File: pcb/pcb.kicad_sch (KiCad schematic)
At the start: 57 parts, among them J1 N!N, J2 Conn_01x02_Socket, J4 Display_nice-view, J8 Conn_01x12_Socket, J9 Conn_01x12_Socket, SW10 Switch, SW11 Switch, SW12 Switch, SW13 Switch, SW14 Switch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

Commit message: small updates
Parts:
- D10, D11, D12, D13, D14, D15, D19, D20, D3, D4, D5, D6, D7, D8, D9: footprint zzkeeb:Diode_1N4148-SOD123-reversible -> zzkeeb:Diode_1N4148-SOD123-reversible-flip3d
- J8, J9: footprint Connector_FFC-FPC:TE_1-84952-2_1x12-1MP_P1.0mm_Horizontal -> zzkeeb:Connector_FFC-12pin-1mm-horizontal
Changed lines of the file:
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@@
       (effects (font (size 1.27 1.27)) (justify right) hide)
     )
-    (property "Footprint" "zzkeeb:Diode_1N4148-SOD123-reversible" (at 66.04 96.52 90)
+    (property "Footprint" "zzkeeb:Diode_1N4148-SOD123-reversible-flip3d" (at 66.04 96.52 90)
       (effects (font (size 1.27 1.27)) hide)
     )
@@
       (effects (font (size 1.27 1.27)) (justify right) hide)
     )
-    (property "Footprint" "zzkeeb:Diode_1N4148-SOD123-reversible" (at 83.82 137.16 90)
+    (property "Footprint" "zzkeeb:Diode_1N4148-SOD123-reversible-flip3d" (at 83.82 137.16 90)
       (effects (font (size 1.27 1.27)) hide)
     )
@@
       (effects (font (size 1.27 1.27)) (justify right) hide)
     )
-    (property "Footprint" "zzkeeb:Diode_1N4148-SOD123-reversible" (at 30.48 96.52 90)
+    (property "Footprint" "zzkeeb:Diode_1N4148-SOD123-reversible-flip3d" (at 30.48 96.52 90)
       (effects (font (size 1.27 1.27)) hide)
     )
@@
       (effects (font (size 1.27 1.27)) (justify right) hide)
     )
-    (property "Footprint" "zzkeeb:Diode_1N4148-SOD123-reversible" (at 30.48 116.84 90)
+    (property "Footprint" "zzkeeb:Diode_1N4148-SOD123-reversible-flip3d" (at 30.48 116.84 90)
       (effects (font (size 1.27 1.27)) hide)
     )
@@
       (effects (font (size 1.27 1.27)) (justify right) hide)
     )
-    (property "Footprint" "zzkeeb:Diode_1N4148-SOD123-reversible" (at 66.04 116.84 90)
+    (property "Footprint" "zzkeeb:Diode_1N4148-SOD123-reversible-flip3d" (at 66.04 116.84 90)
       (effects (font (size 1.27 1.27)) hide)
     )
@@
       (effects (font (size 1.27 1.27)) (justify right) hide)
     )
-    (property "Footprint" "zzkeeb:Diode_1N4148-SOD123-reversible" (at 66.04 137.16 90)
+    (property "Footprint" "zzkeeb:Diode_1N4148-SOD123-reversible-flip3d" (at 66.04 137.16 90)
       (effects (font (size 1.27 1.27)) hide)
     )
@@
       (effects (font (size 1.27 1.27)) (justify right) hide)
     )
-    (property "Footprint" "zzkeeb:Diode_1N4148-SOD123-reversible" (at 48.26 116.84 90)
+    (property "Footprint" "zzkeeb:Diode_1N4148-SOD123-reversible-flip3d" (at 48.26 116.84 90)
       (effects (font (size 1.27 1.27)) hide)
     )
@@
       (effects (font (size 1.27 1.27)) (justify left))
     )
-    (property "Footprint" "Connector_FFC-FPC:TE_1-84952-2_1x12-1MP_P1.0mm_Horizontal" (at 196.85 83.82 0)
+    (property "Footprint" "zzkeeb:Connector_FFC-12pin-1mm-horizontal" (at 196.85 83.82 0)
       (effects (font (size 1.27 1.27)) hide)
     )
@@
       (effects (font (size 1.27 1.27)) (justify right) hide)
     )
-    (property "Footprint" "zzkeeb:Diode_1N4148-SOD123-reversible" (at 48.26 96.52 90)
+    (property "Footprint" "zzkeeb:Diode_1N4148-SOD123-reversible-flip3d" (at 48.26 96.52 90)
       (effects (font (size 1.27 1.27)) hide)
     )
@@
       (effects (font (size 1.27 1.27)) (justify right) hide)
     )
-    (property "Footprint" "zzkeeb:Diode_1N4148-SOD123-reversible" (at 30.48 137.16 90)
+    (property "Footprint" "zzkeeb:Diode_1N4148-SOD123-reversible-flip3d" (at 30.48 137.16 90)
       (effects (font (size 1.27 1.27)) hide)
     )
@@
       (effects (font (size 1.27 1.27)) (justify left))
     )
-    (property "Footprint" "Connector_FFC-FPC:TE_1-84952-2_1x12-1MP_P1.0mm_Horizontal" (at 245.11 83.82 0)
+    (property "Footprint" "zzkeeb:Connector_FFC-12pin-1mm-horizontal" (at 245.11 83.82 0)
       (effects (font (size 1.27 1.27)) hide)
     )
@@
       (effects (font (size 1.27 1.27)) (justify right) hide)
     )
-    (property "Footprint" "zzkeeb:Diode_1N4148-SOD123-reversible" (at 83.82 96.52 90)
+    (property "Footprint" "zzkeeb:Diode_1N4148-SOD123-reversible-flip3d" (at 83.82 96.52 90)
       (effects (font (size 1.27 1.27)) hide)
     )
@@
       (effects (font (size 1.27 1.27)) (justify right) hide)
     )
-    (property "Footprint" "zzkeeb:Diode_1N4148-SOD123-reversible" (at 83.82 157.48 90)
+    (property "Footprint" "zzkeeb:Diode_1N4148-SOD123-reversible-flip3d" (at 83.82 157.48 90)
       (effects (font (size 1.27 1.27)) hide)
     )
@@
       (effects (font (size 1.27 1.27)) (justify right) hide)
     )
-    (property "Footprint" "zzkeeb:Diode_1N4148-SOD123-reversible" (at 101.6 96.52 90)
+    (property "Footprint" "zzkeeb:Diode_1N4148-SOD123-reversible-flip3d" (at 101.6 96.52 90)
       (effects (font (size 1.27 1.27)) hide)
     )
@@
       (effects (font (size 1.27 1.27)) (justify right) hide)
     )
-    (property "Footprint" "zzkeeb:Diode_1N4148-SOD123-reversible" (at 48.26 157.48 90)
+    (property "Footprint" "zzkeeb:Diode_1N4148-SOD123-reversible-flip3d" (at 48.26 157.48 90)
       (effects (font (size 1.27 1.27)) hide)
     )
@@
       (effects (font (size 1.27 1.27)) (justify right) hide)
     )
-    (property "Footprint" "zzkeeb:Diode_1N4148-SOD123-reversible" (at 101.6 116.84 90)
+    (property "Footprint" "zzkeeb:Diode_1N4148-SOD123-reversible-flip3d" (at 101.6 116.84 90)
       (effects (font (size 1.27 1.27)) hide)
     )
@@
       (effects (font (size 1.27 1.27)) (justify right) hide)
     )
-    (property "Footprint" "zzkeeb:Diode_1N4148-SOD123-reversible" (at 66.04 157.48 90)
+    (property "Footprint" "zzkeeb:Diode_1N4148-SOD123-reversible-flip3d" (at 66.04 157.48 90)
       (effects (font (size 1.27 1.27)) hide)
     )
@@
       (effects (font (size 1.27 1.27)) (justify right) hide)
     )
-    (property "Footprint" "zzkeeb:Diode_1N4148-SOD123-reversible" (at 83.82 116.84 90)
+    (property "Footprint" "zzkeeb:Diode_1N4148-SOD123-reversible-flip3d" (at 83.82 116.84 90)
       (effects (font (size 1.27 1.27)) hide)
     )
@@
       (effects (font (size 1.27 1.27)) (justify right) hide)
     )
-    (property "Footprint" "zzkeeb:Diode_1N4148-SOD123-reversible" (at 101.6 157.48 90)
+    (property "Footprint" "zzkeeb:Diode_1N4148-SOD123-reversible-flip3d" (at 101.6 157.48 90)
       (effects (font (size 1.27 1.27)) hide)
     )
@@
       (effects (font (size 1.27 1.27)) (justify right) hide)
     )
-    (property "Footprint" "zzkeeb:Diode_1N4148-SOD123-reversible" (at 48.26 137.16 90)
+    (property "Footprint" "zzkeeb:Diode_1N4148-SOD123-reversible-flip3d" (at 48.26 137.16 90)
       (effects (font (size 1.27 1.27)) hide)
     )
@@
       (effects (font (size 1.27 1.27)) (justify right) hide)
     )
-    (property "Footprint" "zzkeeb:Diode_1N4148-SOD123-reversible" (at 101.6 137.16 90)
+    (property "Footprint" "zzkeeb:Diode_1N4148-SOD123-reversible-flip3d" (at 101.6 137.16 90)
       (effects (font (size 1.27 1.27)) hide)
     )
@@
       (effects (font (size 1.27 1.27)) (justify right) hide)
     )
-    (property "Footprint" "zzkeeb:Diode_1N4148-SOD123-reversible" (at 30.48 157.48 90)
-      (effects (font (size 1.27 1.27)) hide)
-    )
+    (property "Footprint" "zzkeeb:Diode_1N4148-SOD123-reversible-flip3d" (at 30.48 157.48 90)
+      (effects (font (size 1.27 1.27)) hide)
+    )

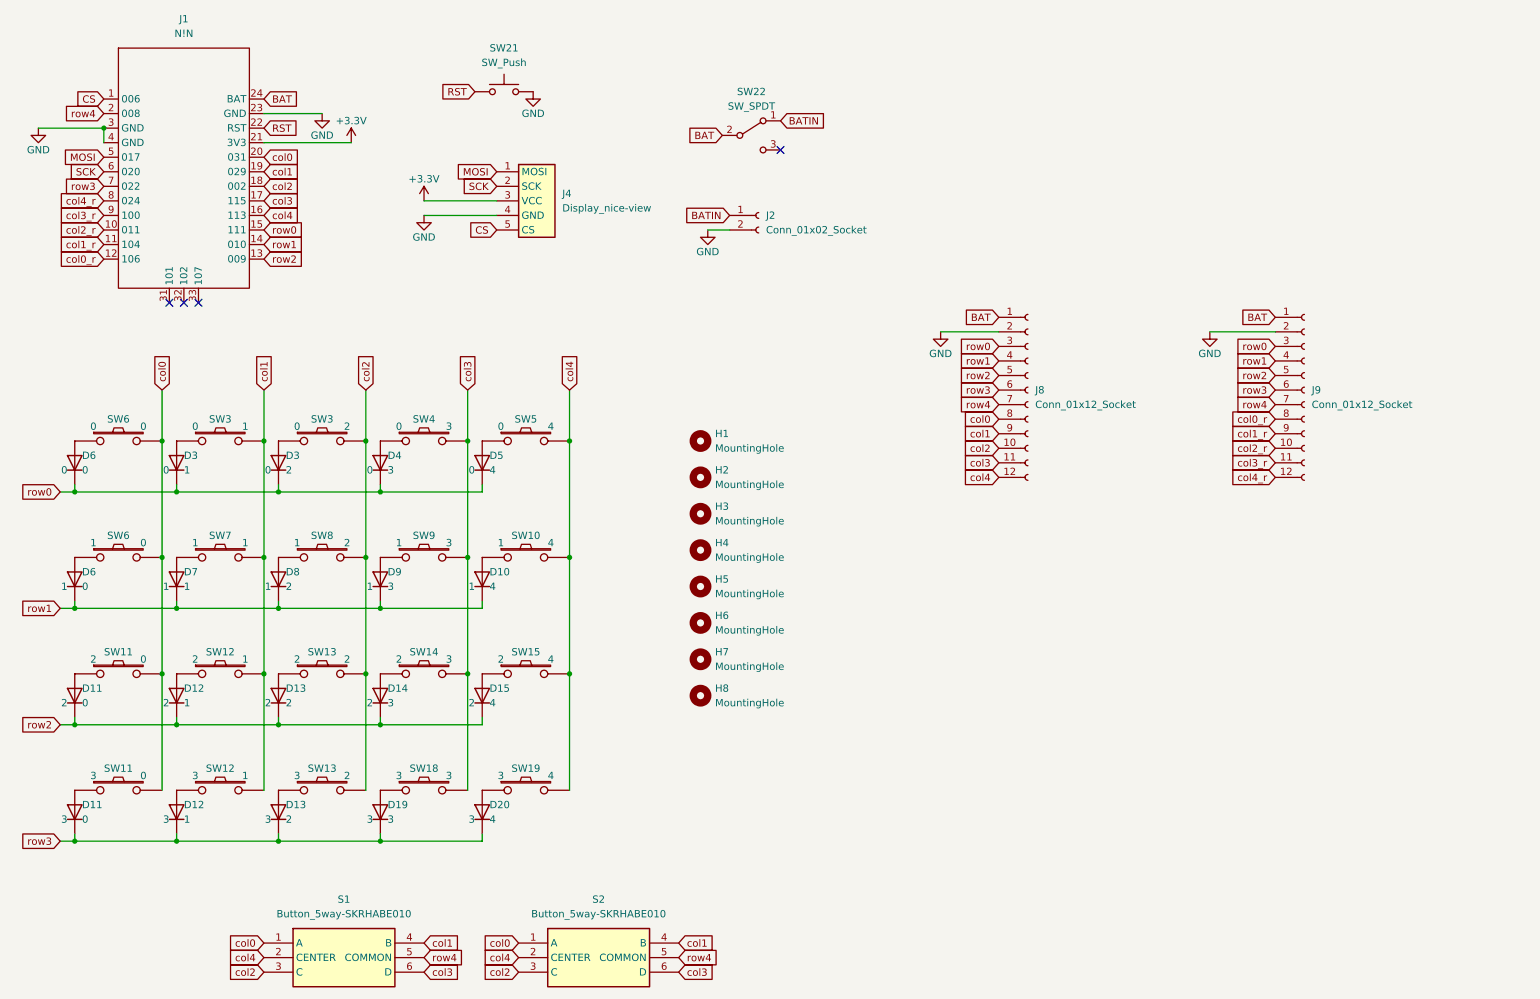
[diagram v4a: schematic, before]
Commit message: move mcu to right, add encoder
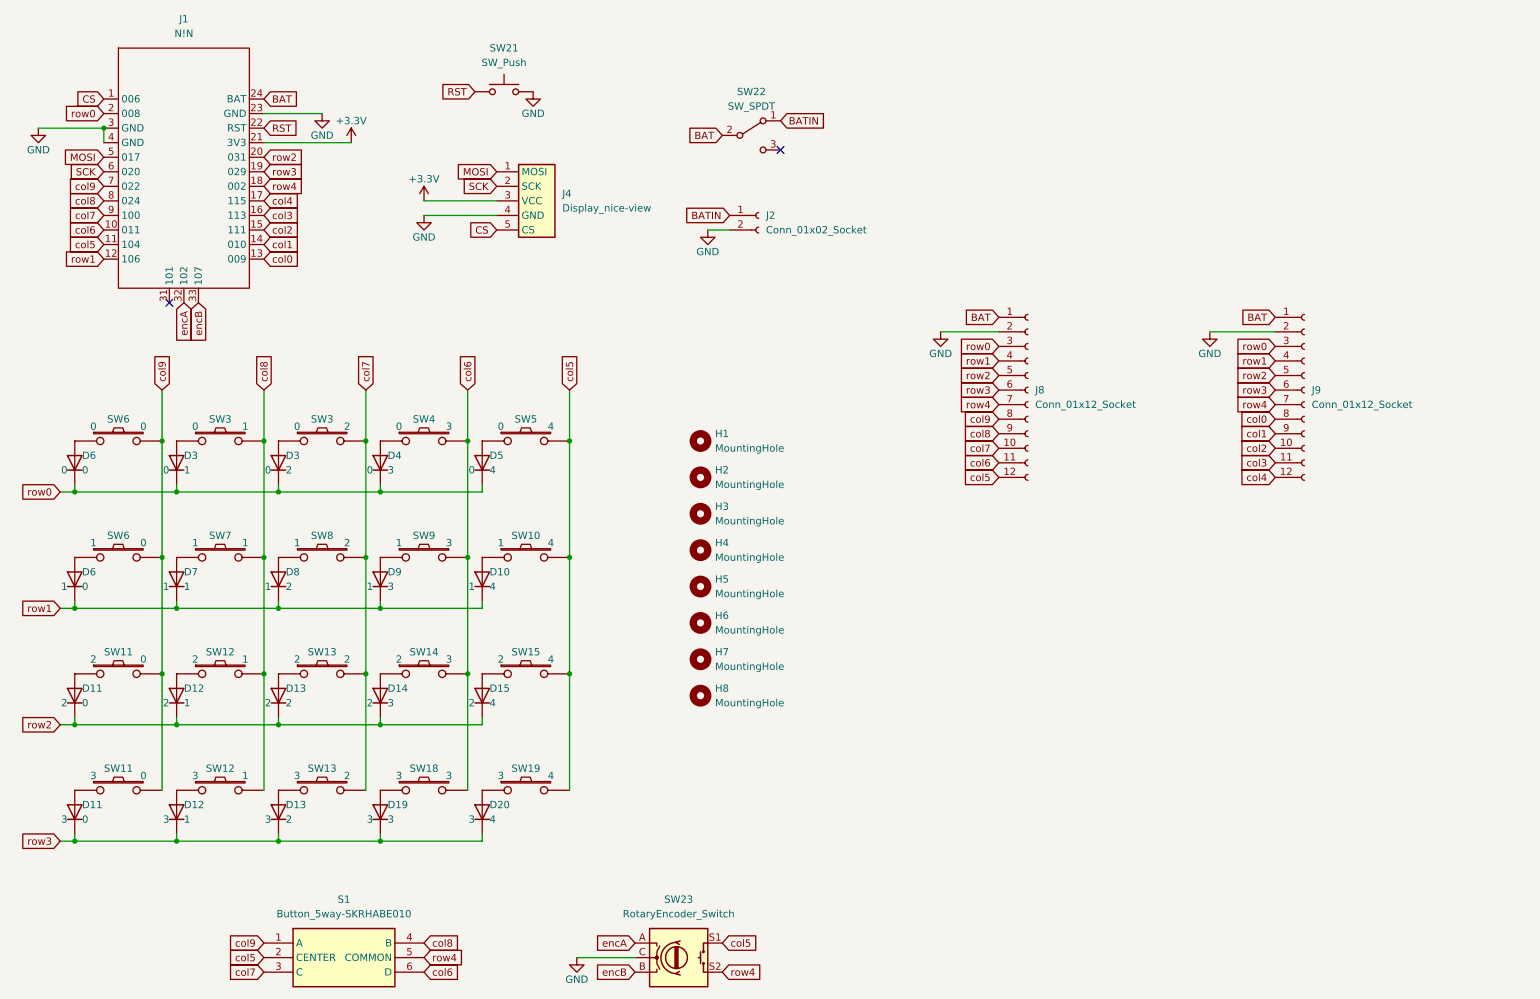
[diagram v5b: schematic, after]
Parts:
- removed S2: Button_5way-SKRHABE010, zzkeeb:Button_5way-SKRHABE010, symbol zzkeeb:Button_5way-SKRHABE010
- added SW23: RotaryEncoder_Switch, zzkeeb:RotaryEncoder_EC11, symbol Device:RotaryEncoder_Switch
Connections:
- net GND: now also SW23.C
- net col0: now also J1.13 (009), J9.8 (Pin_8); no longer J1.20 (031), J8.8 (Pin_8), S1.1 (A), SW11.2, SW11.2, SW6.2, SW6.2
- net col1: now also J1.14 (010), J9.9 (Pin_9); no longer J1.19 (029), J8.9 (Pin_9), S1.4 (B), SW12.2, SW12.2, SW3.2, SW7.2
- net col2: now also J1.15 (111), J9.10 (Pin_10); no longer J1.18 (002), J8.10 (Pin_10), S1.3 (C), SW13.2, SW13.2, SW3.2, SW8.2
- net col3: now also J1.16 (113), J9.11 (Pin_11); no longer J1.17 (115), J8.11 (Pin_11), S1.6 (D), SW14.2, SW18.2, SW4.2, SW9.2
- net col4: now also J1.17 (115), J9.12 (Pin_12); no longer J1.16 (113), J8.12 (Pin_12), S1.2 (CENTER), SW10.2, SW15.2, SW19.2, SW5.2
- net row0: now also J1.2 (008); no longer J1.15 (111)
- net row1: now also J1.12 (106); no longer J1.14 (010)
- net row2: now also J1.20 (031); no longer J1.13 (009)
- net row3: now also J1.19 (029); no longer J1.7 (022)
- net row4: now also J1.18 (002), SW23.S2; no longer J1.2 (008)
- net encA: now reaches J1.32 (102)
- net encA: now also SW23.A
- net encB: now reaches J1.33 (107)
- net encB: now also SW23.B
- removed net col0_r: J1.12 (106), J9.8 (Pin_8)
- net col1_r renamed col5
- net col5: now also J8.12 (Pin_12), S1.2 (CENTER), SW10.2, SW15.2, SW19.2, SW5.2, SW23.S1; no longer J9.9 (Pin_9)
- net col2_r renamed col6
- net col6: now also J8.11 (Pin_11), S1.6 (D), SW14.2, SW18.2, SW4.2, SW9.2; no longer J9.10 (Pin_10)
- net col3_r renamed col7
- net col7: now also J8.10 (Pin_10), S1.3 (C), SW13.2, SW13.2, SW3.2, SW8.2; no longer J9.11 (Pin_11)
- net col4_r renamed col8
- net col8: now also J8.9 (Pin_9), S1.4 (B), SW12.2, SW12.2, SW3.2, SW7.2; no longer J9.12 (Pin_12)
- new net col9: J1.7 (022), J8.8 (Pin_8), S1.1 (A), SW11.2, SW11.2, SW6.2, SW6.2
- no-connect marks 4 -> 2

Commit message: pcb 0.3
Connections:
- net BAT: now also J9.12 (Pin_12); no longer J9.1 (Pin_1)
- net GND: now also J9.11 (Pin_11); no longer J9.2 (Pin_2)
- net col0: now also J9.5 (Pin_5); no longer J9.8 (Pin_8)
- net col1: now also J9.4 (Pin_4); no longer J9.9 (Pin_9)
- net col2: now also J9.3 (Pin_3); no longer J9.10 (Pin_10)
- net col3: now also J9.2 (Pin_2); no longer J9.11 (Pin_11)
- net col4: now also J9.1 (Pin_1); no longer J9.12 (Pin_12)
- net row0: now also J8.7 (Pin_7), J9.6 (Pin_6); no longer J8.3 (Pin_3), J9.3 (Pin_3)
- net row1: now also J8.6 (Pin_6), J9.7 (Pin_7); no longer J8.4 (Pin_4), J9.4 (Pin_4)
- net row2: now also J1.18 (002), J9.8 (Pin_8); no longer J1.20 (031), J9.5 (Pin_5)
- net row3: now also J8.4 (Pin_4), J9.9 (Pin_9); no longer J8.6 (Pin_6), J9.6 (Pin_6)
- net row4: now also J1.20 (031), J8.3 (Pin_3), J9.10 (Pin_10); no longer J1.18 (002), J8.7 (Pin_7), J9.7 (Pin_7)

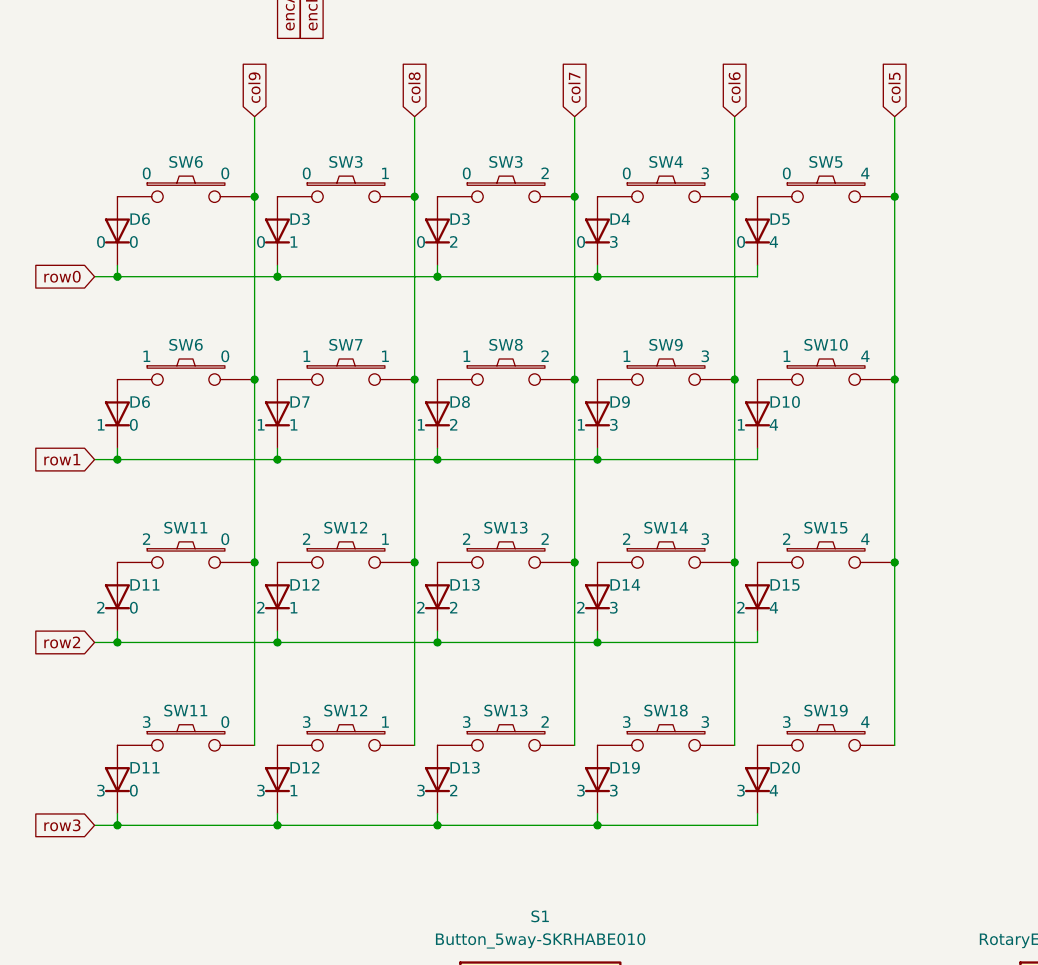
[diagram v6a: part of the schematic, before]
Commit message: fix pcb silkscreen
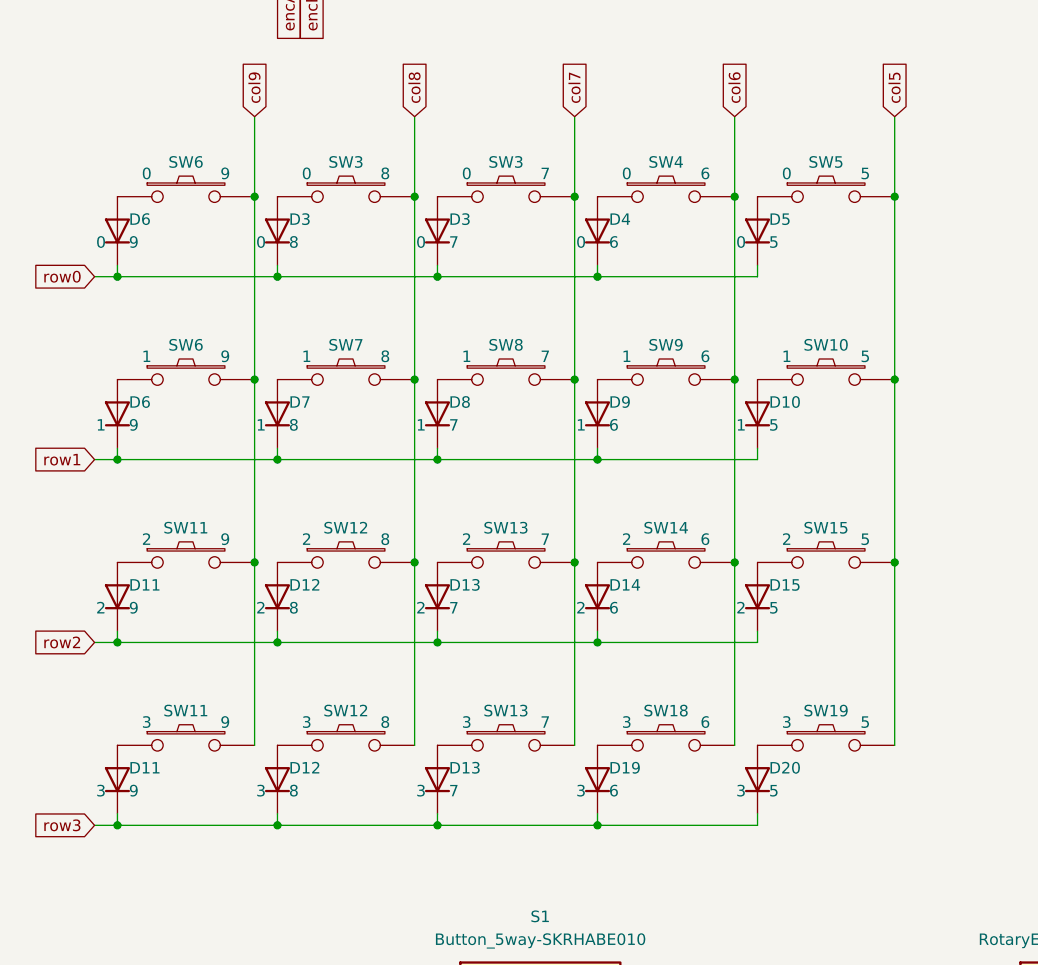
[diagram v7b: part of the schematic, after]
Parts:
- D10, D15, D20, D5, SW10, SW15, SW19, SW5: col 4 -> 5
- D11, D6, SW11, SW6: col 0 -> 9
- D12, D3, D7, SW12, SW3, SW7: col 1 -> 8
- D13, D3, D8, SW13, SW3, SW8: col 2 -> 7
- D14, D19, D4, D9, SW14, SW18, SW4, SW9: col 3 -> 6
